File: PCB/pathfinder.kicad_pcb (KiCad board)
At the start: 2 copper layers, 150 x 100 mm, 18 parts, among them SW1 SW_Push, SW2 SW_Push, SW3 SW_Push, SW4 SW_Push, SW5 SW_Push, SW6 SW_Push, SW7 SW_Push, SW8 SW_Push, SW9 SW_Push, U2 XIAO-RP2040-DIP

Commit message: pcb change
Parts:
- moved U2 68.6 mm to (206.5, 130.3)
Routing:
- net POWER: track 33.2 -> 103.6 mm
- net GAS: track 36.7 -> 92.5 mm
- net BRAKE: track 43.5 -> 86.7 mm
- net RIGHT: track 26.8 -> 69.5 mm
- net Drift Indicator: track 48.4 -> 88.0 mm
- net LEFT: track 68.3 -> 106.6 mm, vias 0 -> 2
- net CHECKPOINT: track 52.0 -> 88.4 mm
- net AK80: track 75.3 -> 42.6 mm
- net AK60: track 87.7 -> 62.7 mm
- net GND: track 296.2 -> 313.4 mm, vias 0 -> 1
- net AK40: track 72.3 -> 59.9 mm, vias 0 -> 2
- net RESTART: track 48.1 -> 42.3 mm, vias 0 -> 2

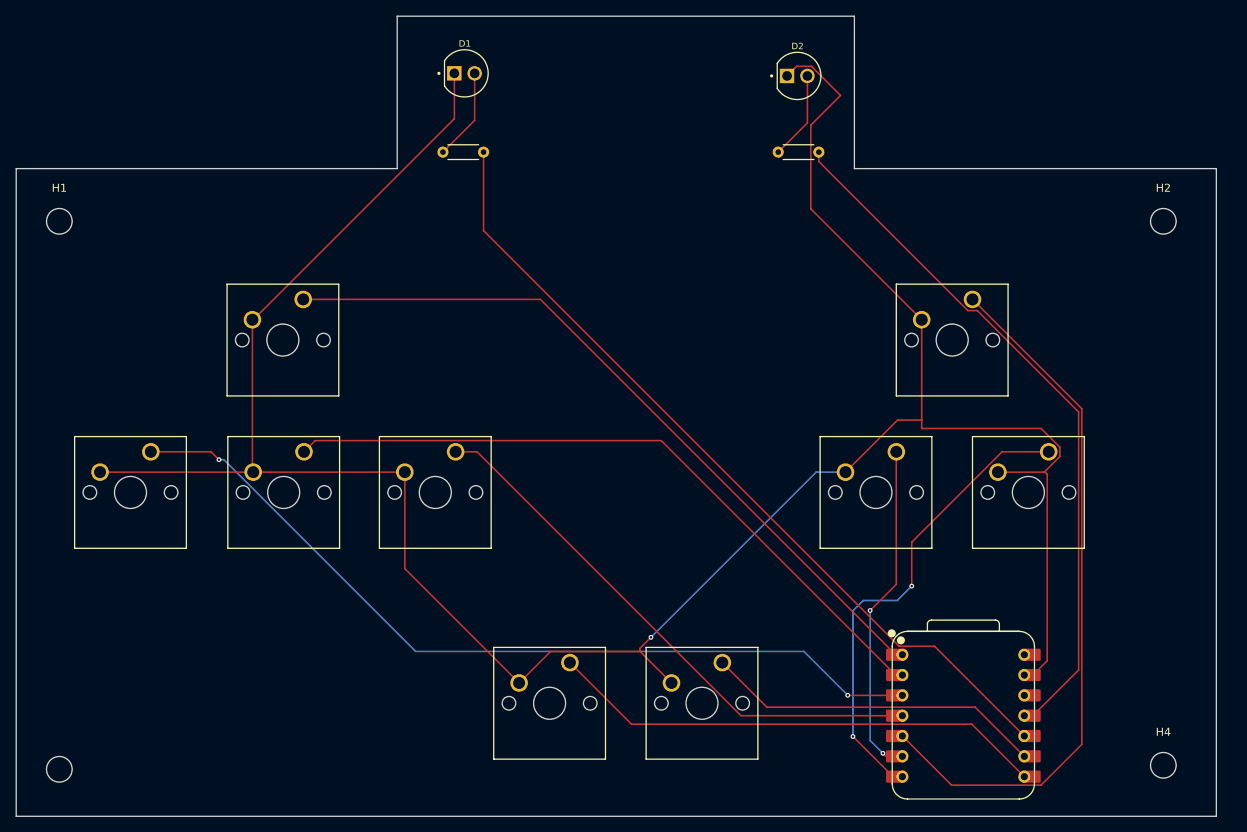
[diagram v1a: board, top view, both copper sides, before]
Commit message: rotated the xiao
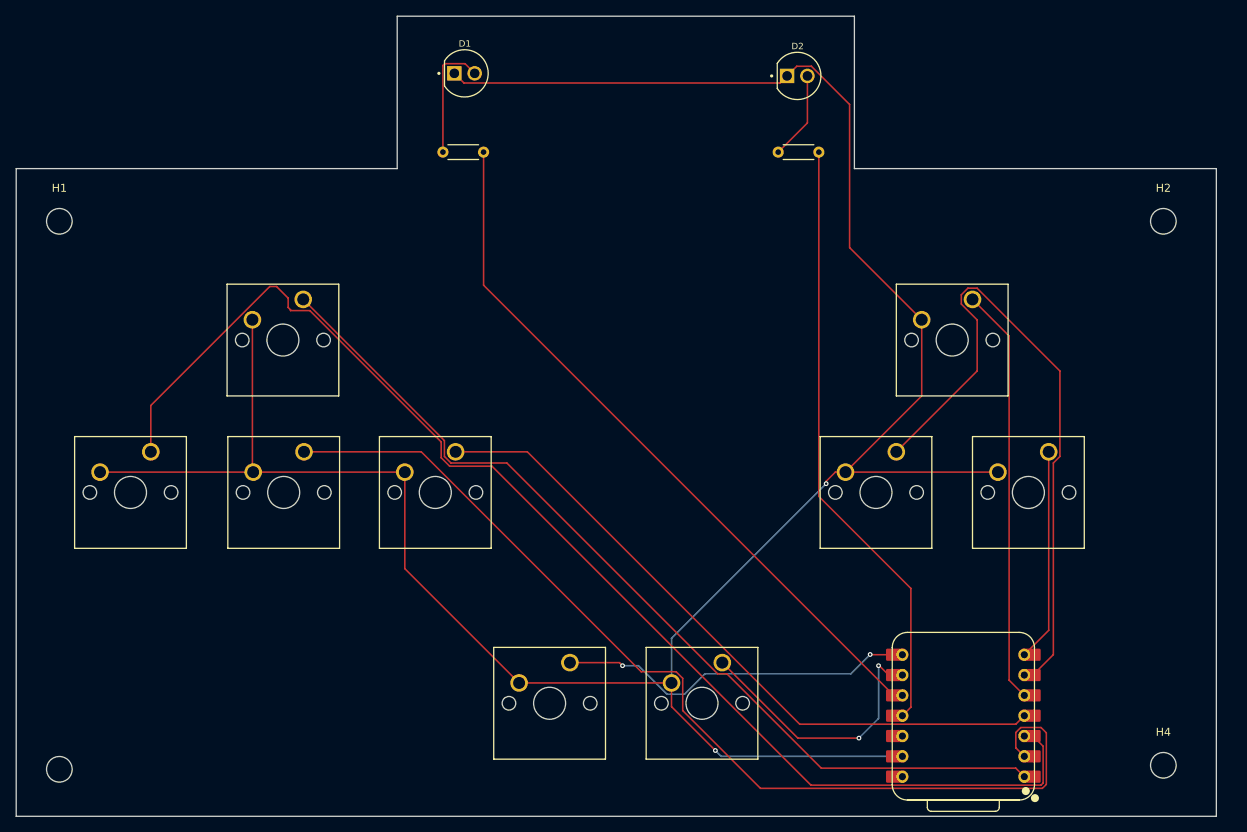
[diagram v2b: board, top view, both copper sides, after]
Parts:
- turned U2 to 180 degrees
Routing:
- net LEFT: track 106.6 -> 158.8 mm, vias 2 -> 0
- net BRAKE: track 86.7 -> 127.0 mm
- net RESTART: track 42.3 -> 82.1 mm, vias 2 -> 0
- net CHECKPOINT: track 88.4 -> 52.2 mm
- net AK40: track 59.9 -> 26.6 mm, vias 2 -> 0
- net GAS: track 92.5 -> 116.0 mm
- net AK60: track 62.7 -> 45.3 mm, vias 0 -> 2
- net RIGHT: track 69.5 -> 85.6 mm
- net POWER: track 103.6 -> 90.2 mm
- net Drift Indicator: track 88.0 -> 75.7 mm
- net GND: track 313.4 -> 304.5 mm, vias 1 -> 2
- net AK80: track 42.6 -> 34.5 mm, vias 0 -> 2
- net Net-(D1-PadA): track 11.5 -> 15.4 mm

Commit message: gerber and pcb
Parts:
- removed H1, H3: MountingHole, MountingHole:MountingHole_3.2mm_M3
- added HSMALL1: MountingHole, custom_footprints:mouse-bite-2mm-slot, F.Cu at (179.2, 117.6)
- added HSMALL2: MountingHole, custom_footprints:mouse-bite-2mm-slot, F.Cu at (179.3, 109.7)
- added U3: XIAO-RP2040-DIP, footprints:XIAO-Generic-Hybrid-14P-2.54-21X17.8MM, F.Cu at (209.0, 119.7)
- D1: value L08R5000Q1 -> POWER
- D2: value L08R5000Q1 -> Drift
- SW1: value SW_Push -> GAS
- SW2: value SW_Push -> BRAKE
- SW3: value SW_Push -> LEFT
- SW4: value SW_Push -> RIGHT
- SW5: value SW_Push -> CHECKPOINT
- SW6: value SW_Push -> RESTART
- SW7: value SW_Push -> AK40
- SW8: value SW_Push -> AK60
- SW9: value SW_Push -> AK80
- U2: footprint mito-keyboard mito-simplified main Seeed Studio XIAO Series Library:XIAO-RP2040-DIP -> footprints:XIAO-Generic-Hybrid-14P-2.54-21X17.8MM
- moved U2 77.8 mm to (129.4, 120.5)
- moved HBIG1 72.9 mm to (161.2, 87.8)
- moved HBIG2 61.8 mm to (192.7, 88.4)
- moved SW1 47.2 mm to (152.5, 115.9)
- moved D1 43.7 mm to (169.2, 85.8)
- moved R1 39.7 mm to (166.5, 90.6)
- moved D2 35.6 mm to (184.3, 85.9)
- moved R2 30.8 mm to (182.5, 90.7)
- moved SW5 29.3 mm to (230.2, 97.0)
- moved SW2 28.5 mm to (152.6, 96.8)
- moved SW3 28.5 mm to (133.4, 96.8)
- moved SW4 28.5 mm to (171.5, 96.8)
- moved SW9 17.5 mm to (192.1, 116.0)
- moved SW8 16.2 mm to (171.5, 115.9)
- moved SW6 6.01 mm to (192.1, 97.0)
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- renumbered H2 to HBIG1, H4 to HBIG2
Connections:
- U2 pad 10: POWER -> unconnected-(U2-GPIO4/MISO-Pad10)
- U2 pad 11: Drift Indicator -> unconnected-(U2-GPIO3/MOSI-Pad11)
- U2 pad 5: CHECKPOINT -> AK60
- U2 pad 6: RESTART -> POWER
- U2 pad 7: AK40 -> unconnected-(U2-GPIO0/TX-Pad7)
- U2 pad 8: AK60 -> unconnected-(U2-GPIO1/RX-Pad8)
- U2 pad 9: AK80 -> unconnected-(U2-GPIO2/SCK-Pad9)
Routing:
- net LEFT: track 158.8 -> 27.8 mm
- net GND: track 304.5 -> 208.5 mm, vias 2 -> 0
- net GAS: track 116.0 -> 20.6 mm
- net BRAKE: track 127.0 -> 36.3 mm
- net RESTART: track 82.1 -> 37.9 mm
- net POWER: track 90.2 -> 50.9 mm, vias 0 -> 1
- net Drift Indicator: track 75.7 -> 40.2 mm
- net RIGHT: track 85.6 -> 54.7 mm
- net CHECKPOINT: track 52.2 -> 42.2 mm, vias 0 -> 1
- net Net-(D1-PadA): track 15.4 -> 6.49 mm
- net AK60: track 45.3 -> 36.6 mm, vias 2 -> 1
- net AK80: track 34.5 -> 27.0 mm, vias 2 -> 1
- net Net-(D2-PadA): track 11.0 -> 6.01 mm
- net AK40: track 26.6 -> 31.4 mm, vias 0 -> 3
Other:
- board size 150 x 100 mm -> 119.1 x 48 mm

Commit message: prod, cad,
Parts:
- removed HSMALL1: MountingHole, custom_footprints:mouse-bite-2mm-slot
- moved R2 2.75 mm to (185.2, 90.5)
- moved SW5 2.75 mm to (233.0, 96.8)
- moved SW6 2.75 mm to (194.9, 96.8)
- moved SW7 2.75 mm to (213.9, 96.8)
- moved SW9 2.75 mm to (194.9, 115.9)
- moved U3 2.75 mm to (211.7, 119.5)
- moved HBIG2 2.75 mm to (195.4, 88.2)
- moved D2 2.75 mm to (187.0, 85.8)
- moved HSMALL2 0.37 mm to (179.6, 109.5)
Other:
- board size 119.1 x 48 mm -> 121.8 x 48 mm
